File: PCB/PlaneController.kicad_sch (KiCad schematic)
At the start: 13 parts, among them J1 Conn_01x06_Pin, J2 Conn_01x04_Pin, J3 Conn_01x02, M1 Motor_Servo, M2 Motor_Servo, M3 Motor_Servo, M4 Motor_Servo, M5 Motor_Servo

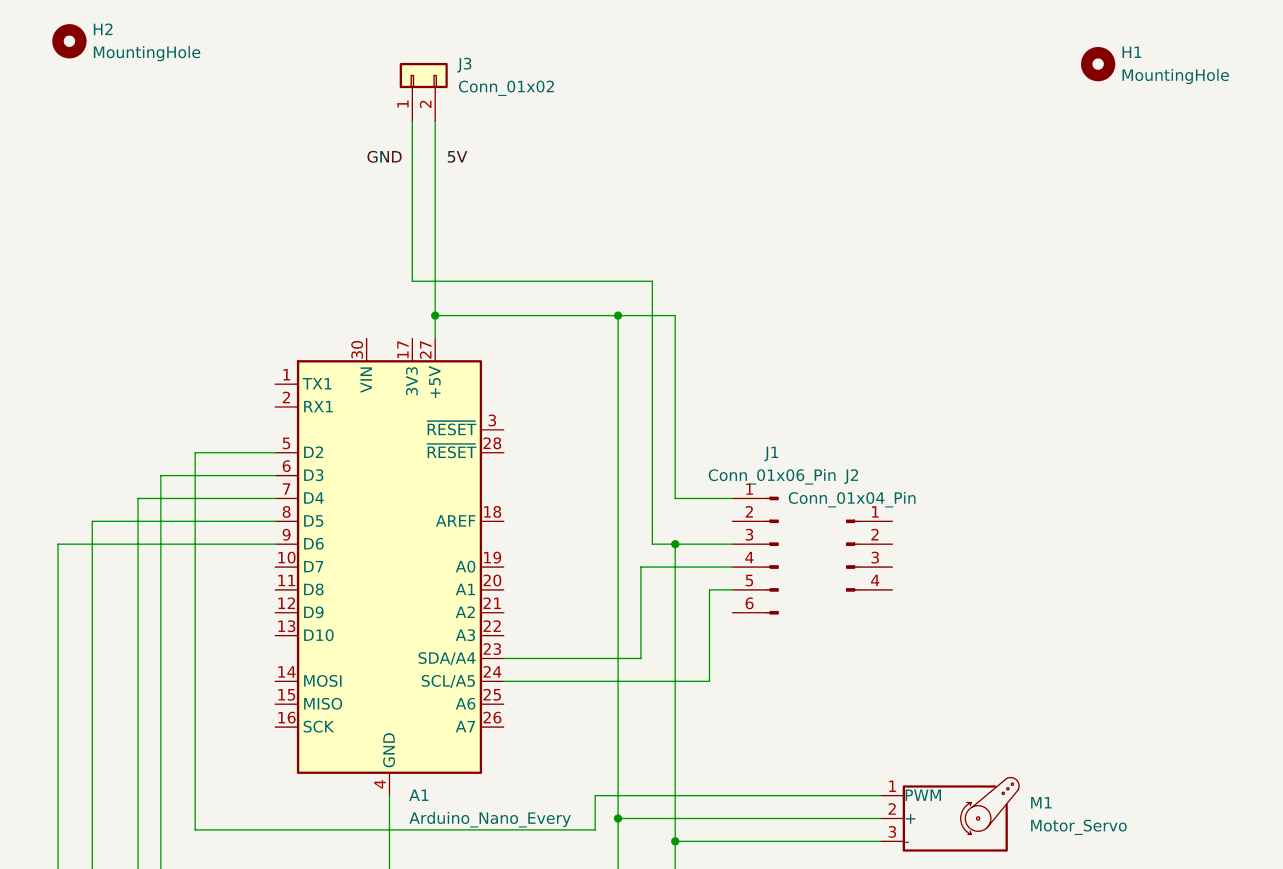
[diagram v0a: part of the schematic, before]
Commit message: Add RX and TX connections to connect to receiver via iBUS
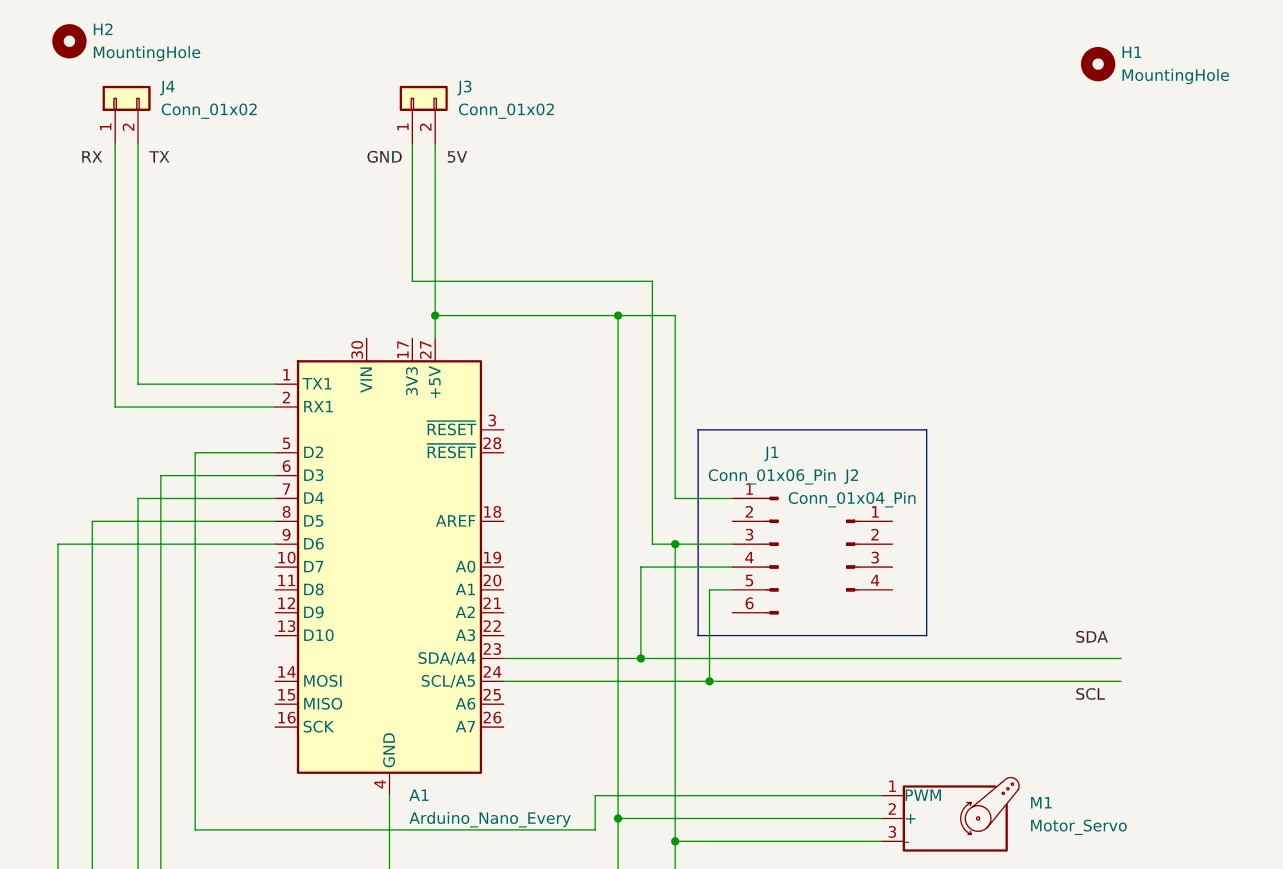
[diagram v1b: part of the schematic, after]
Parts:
- added J4: Conn_01x02, Connector_PinHeader_2.54mm:PinHeader_1x02_P2.54mm_Vertical, symbol Connector_Generic:Conn_01x02
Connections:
- net at A1.1 (TX1): now also J4.2 (Pin_2)
- net at A1.2 (RX1): now also J4.1 (Pin_1)
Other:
- moved on the sheet: J3
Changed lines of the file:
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@@
 	(paper "A4")
+	(junction
+		(at 107.95 116.84)
+		(diameter 0)
+		(color 0 0 0 0)
+	)
 	(junction
 		(at 104.14 101.6)
@@
 	)
 	(junction
+		(at 100.33 114.3)
+		(diameter 0)
+		(color 0 0 0 0)
+	)
+	(junction
 		(at 97.79 177.8)
 		(diameter 0)
@@
 	(wire
 		(pts
+			(xy 41.91 57.15) (xy 41.91 86.36)
+		)
+		(stroke
+			(width 0)
+			(type default)
+		)
+	)
+	(wire
+		(pts
 			(xy 127 142.24) (xy 46.99 142.24)
 		)
@@
 	(wire
 		(pts
+			(xy 59.69 86.36) (xy 41.91 86.36)
+		)
+		(stroke
+			(width 0)
+			(type default)
+		)
+	)
+	(wire
+		(pts
 			(xy 97.79 153.67) (xy 127 153.67)
 		)
@@
 	(wire
 		(pts
+			(xy 59.69 83.82) (xy 44.45 83.82)
+		)
+		(stroke
+			(width 0)
+			(type default)
+		)
+	)
+	(wire
+		(pts
 			(xy 104.14 180.34) (xy 127 180.34)
 		)
@@
 	(wire
 		(pts
-			(xy 74.93 54.61) (xy 74.93 72.39)
+			(xy 74.93 57.15) (xy 74.93 72.39)
 		)
 		(stroke
@@
 	(wire
 		(pts
+			(xy 44.45 57.15) (xy 44.45 83.82)
+		)
+		(stroke
+			(width 0)
+			(type default)
+		)
+	)
+	(wire
+		(pts
 			(xy 95.25 129.54) (xy 127 129.54)
 		)
@@
 	(wire
 		(pts
+			(xy 100.33 114.3) (xy 153.67 114.3)
+		)
+		(stroke
+			(width 0)
+			(type default)
+		)
+	)
+	(wire
+		(pts
 			(xy 95.25 129.54) (xy 95.25 133.35)
 		)
@@
 	(wire
 		(pts
+			(xy 107.95 116.84) (xy 153.67 116.84)
+		)
+		(stroke
+			(width 0)
+			(type default)
+		)
+	)
+	(wire
+		(pts
 			(xy 104.14 180.34) (xy 104.14 190.5)
 		)
@@
 	(wire
 		(pts
-			(xy 77.47 54.61) (xy 77.47 76.2)
+			(xy 77.47 57.15) (xy 77.47 76.2)
 		)
 		(stroke
@@
 		)
 	)
-	(label "5V"
-		(at 78.74 59.69 0)
+	(rectangle
+		(start 106.68 88.9)
+		(end 132.08 111.76)
+		(stroke
+			(width 0)
+			(type default)
+		)
+		(fill
+			(type none)
+		)
+	)
+	(label "SCL"
+		(at 148.59 119.38 0)
 		(fields_autoplaced yes)
 		(effects
@@
 		)
 	)
+	(label "5V"
+		(at 78.74 59.69 0)
+		(fields_autoplaced yes)
+		(effects
+			(font
+				(size 1.27 1.27)
+			)
+			(justify left bottom)
+		)
+	)
 	(label "GND"
 		(at 69.85 59.69 0)
+		(fields_autoplaced yes)
+		(effects
+			(font
+				(size 1.27 1.27)
+			)
+			(justify left bottom)
+		)
+	)
+	(label "TX"
+		(at 45.72 59.69 0)
+		(fields_autoplaced yes)
+		(effects
+			(font
+				(size 1.27 1.27)
+			)
+			(justify left bottom)
+		)
+	)
+	(label "RX"
+		(at 38.1 59.69 0)
+		(fields_autoplaced yes)
+		(effects
+			(font
+				(size 1.27 1.27)
+			)
+			(justify left bottom)
+		)
+	)
+	(label "SDA"
+		(at 148.59 113.03 0)
 		(fields_autoplaced yes)
 		(effects
@@
 	(symbol
 		(lib_id "Connector_Generic:Conn_01x02")
-		(at 74.93 49.53 90)
+		(at 74.93 52.07 90)
 		(unit 1)
 		(exclude_from_sim no)
@@
 		(fields_autoplaced yes)
 		(property "Reference" "J3"
-			(at 80.01 48.2599 90)
+			(at 80.01 50.7999 90)
 			(effects
 				(font
@@
 		)
 		(property "Value" "Conn_01x02"
-			(at 80.01 50.7999 90)
+			(at 80.01 53.3399 90)
 			(effects
 				(font
@@
 		)
 		(property "Footprint" "Connector_PinHeader_2.54mm:PinHeader_1x02_P2.54mm_Vertical"
-			(at 74.93 49.53 0)
+			(at 74.93 52.07 0)
 			(effects
 				(font
@@
 		)
 		(property "Datasheet" "~"
-			(at 74.93 49.53 0)
+			(at 74.93 52.07 0)
 			(effects
 				(font
@@
 		)
 		(property "Description" "Generic connector, single row, 01x02, script generated (kicad-library-utils/schlib/autogen/connector/)"
-			(at 74.93 49.53 0)
+			(at 74.93 52.07 0)
 			(effects
 				(font
@@
 					(unit 1)
 				)
+			)
+		)
+	)
+	(symbol
+		(lib_id "Connector_Generic:Conn_01x02")
+		(at 41.91 52.07 90)
+		(unit 1)
+		(exclude_from_sim no)
+		(in_bom yes)
+		(on_board yes)
+		(dnp no)
+		(fields_autoplaced yes)
+		(property "Reference" "J4"
+			(at 46.99 50.7999 90)
+			(effects
+				(font
+					(size 1.27 1.27)
+				)
+				(justify right)
+			)
+		)
+		(property "Value" "Conn_01x02"
+			(at 46.99 53.3399 90)
+			(effects
+				(font
+					(size 1.27 1.27)
+				)
+				(justify right)
+			)
+		)
+		(property "Footprint" "Connector_PinHeader_2.54mm:PinHeader_1x02_P2.54mm_Vertical"
+			(at 41.91 52.07 0)
+			(effects
+				(font
+					(size 1.27 1.27)
+				)
+				(hide yes)
+			)
+		)
+		(property "Datasheet" "~"
+			(at 41.91 52.07 0)
+			(effects
+				(font
+					(size 1.27 1.27)
+				)
+				(hide yes)
+			)
+		)
+		(property "Description" "Generic connector, single row, 01x02, script generated (kicad-library-utils/schlib/autogen/connector/)"
+			(at 41.91 52.07 0)
+			(effects
+				(font
+					(size 1.27 1.27)
+				)
+				(hide yes)
+			)
+		)
+		(pin "1"
+		)
+		(pin "2"
+		)
+		(instances
+			(project "PlaneController"
+				(path "/f475b102-a671-4895-926c-dd521b2271ca"
+					(reference "J4")
+					(unit 1)
+				)

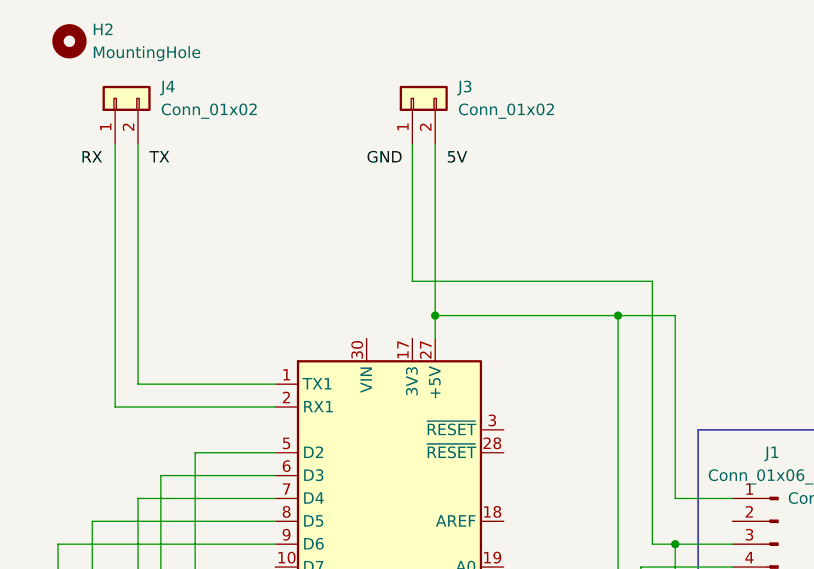
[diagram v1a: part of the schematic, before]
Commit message: Add connection to receiver using 3x1 pin for iBUS, Vcc and GND
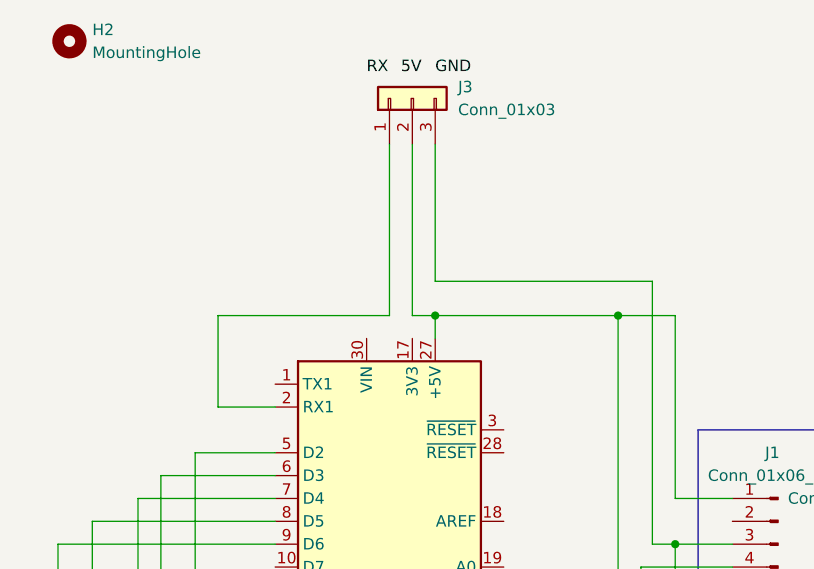
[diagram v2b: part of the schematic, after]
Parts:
- removed J3, J4: Conn_01x02, Connector_PinHeader_2.54mm:PinHeader_1x02_P2.54mm_Vertical, symbol Connector_Generic:Conn_01x02
- added J3: Conn_01x03, Connector_PinHeader_2.54mm:PinHeader_1x03_P2.54mm_Vertical, symbol Connector_Generic:Conn_01x03
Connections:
- net at A1.27 (+5V), J1.1 (Pin_1), M1.2 (+)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: now also J3.2 (Pin_2)
- net at A1.29 (GND), A1.4 (GND), J1.3 (Pin_3)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: now also J3.3 (Pin_3)
- net at A1.2 (RX1): now also J3.1 (Pin_1)
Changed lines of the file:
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@@
+	)
+	(junction
+		(at 77.47 76.2)
+		(diameter 0)
+		(color 0 0 0 0)
 	)
 	(junction
@@
 	)
 	(junction
-		(at 77.47 76.2)
-		(diameter 0)
-		(color 0 0 0 0)
-	)
-	(junction
 		(at 104.14 167.64)
 		(diameter 0)
@@
 	(wire
 		(pts
+			(xy 72.39 57.15) (xy 72.39 76.2)
+		)
+		(stroke
+			(width 0)
+			(type default)
+		)
+	)
+	(wire
+		(pts
 			(xy 97.79 76.2) (xy 77.47 76.2)
 		)
@@
 	(wire
 		(pts
+			(xy 72.39 76.2) (xy 53.34 76.2)
+		)
+		(stroke
+			(width 0)
+			(type default)
+		)
+	)
+	(wire
+		(pts
 			(xy 104.14 167.64) (xy 127 167.64)
 		)
@@
 	(wire
 		(pts
-			(xy 41.91 57.15) (xy 41.91 86.36)
-		)
-		(stroke
-			(width 0)
-			(type default)
-		)
-	)
-	(wire
-		(pts
 			(xy 127 142.24) (xy 46.99 142.24)
 		)
@@
 	(wire
 		(pts
-			(xy 74.93 72.39) (xy 101.6 72.39)
-		)
-		(stroke
-			(width 0)
-			(type default)
-		)
-	)
-	(wire
-		(pts
 			(xy 104.14 156.21) (xy 104.14 167.64)
 		)
@@
 	(wire
 		(pts
-			(xy 59.69 86.36) (xy 41.91 86.36)
+			(xy 74.93 76.2) (xy 77.47 76.2)
 		)
 		(stroke
@@
 	(wire
 		(pts
-			(xy 59.69 83.82) (xy 44.45 83.82)
+			(xy 101.6 72.39) (xy 77.47 72.39)
 		)
 		(stroke
@@
 	(wire
 		(pts
-			(xy 74.93 57.15) (xy 74.93 72.39)
-		)
-		(stroke
-			(width 0)
-			(type default)
-		)
-	)
-	(wire
-		(pts
 			(xy 101.6 101.6) (xy 104.14 101.6)
 		)
@@
 	(wire
 		(pts
-			(xy 44.45 57.15) (xy 44.45 83.82)
+			(xy 74.93 57.15) (xy 74.93 76.2)
 		)
 		(stroke
@@
 	(wire
 		(pts
+			(xy 77.47 57.15) (xy 77.47 72.39)
+		)
+		(stroke
+			(width 0)
+			(type default)
+		)
+	)
+	(wire
+		(pts
 			(xy 100.33 114.3) (xy 153.67 114.3)
 		)
@@
 	(wire
 		(pts
+			(xy 53.34 76.2) (xy 53.34 86.36)
+		)
+		(stroke
+			(width 0)
+			(type default)
+		)
+	)
+	(wire
+		(pts
 			(xy 39.37 162.56) (xy 39.37 99.06)
 		)
@@
 	(wire
 		(pts
+			(xy 53.34 86.36) (xy 59.69 86.36)
+		)
+		(stroke
+			(width 0)
+			(type default)
+		)
+	)
+	(wire
+		(pts
 			(xy 104.14 180.34) (xy 104.14 190.5)
 		)
@@
 		(pts
 			(xy 44.45 96.52) (xy 59.69 96.52)
-		)
-		(stroke
-			(width 0)
-			(type default)
-		)
-	)
-	(wire
-		(pts
-			(xy 77.47 57.15) (xy 77.47 76.2)
 		)
 		(stroke
@@
 	)
 	(label "5V"
-		(at 78.74 59.69 0)
+		(at 73.66 49.53 0)
 		(fields_autoplaced yes)
 		(effects
@@
 	)
 	(label "GND"
-		(at 69.85 59.69 0)
+		(at 77.47 49.53 0)
 		(fields_autoplaced yes)
 		(effects
@@
 		)
 	)
-	(label "TX"
-		(at 45.72 59.69 0)
-		(fields_autoplaced yes)
-		(effects
-			(font
-				(size 1.27 1.27)
-			)
-			(justify left bottom)
-		)
-	)
 	(label "RX"
-		(at 38.1 59.69 0)
+		(at 69.85 49.53 0)
 		(fields_autoplaced yes)
 		(effects
@@
 				(path "/f475b102-a671-4895-926c-dd521b2271ca"
 					(reference "M2")
-					(unit 1)
-				)
-			)
-		)
-	)
-	(symbol
-		(lib_id "Connector_Generic:Conn_01x02")
-		(at 74.93 52.07 90)
-		(unit 1)
-		(exclude_from_sim no)
-		(in_bom yes)
-		(on_board yes)
-		(dnp no)
-		(fields_autoplaced yes)
-		(property "Reference" "J3"
-			(at 80.01 50.7999 90)
-			(effects
-				(font
-					(size 1.27 1.27)
-				)
-				(justify right)
-			)
-		)
-		(property "Value" "Conn_01x02"
-			(at 80.01 53.3399 90)
-			(effects
-				(font
-					(size 1.27 1.27)
-				)
-				(justify right)
-			)
-		)
-		(property "Footprint" "Connector_PinHeader_2.54mm:PinHeader_1x02_P2.54mm_Vertical"
-			(at 74.93 52.07 0)
-			(effects
-				(font
-					(size 1.27 1.27)
-				)
-				(hide yes)
-			)
-		)
-		(property "Datasheet" "~"
-			(at 74.93 52.07 0)
-			(effects
-				(font
-					(size 1.27 1.27)
-				)
-				(hide yes)
-			)
-		)
-		(property "Description" "Generic connector, single row, 01x02, script generated (kicad-library-utils/schlib/autogen/connector/)"
-			(at 74.93 52.07 0)
-			(effects
-				(font
-					(size 1.27 1.27)
-				)
-				(hide yes)
-			)
-		)
-		(pin "1"
-		)
-		(pin "2"
-		)
-		(instances
-			(project ""
-				(path "/f475b102-a671-4895-926c-dd521b2271ca"
-					(reference "J3")
 					(unit 1)
 				)
@@
 	)
 	(symbol
-		(lib_id "Connector_Generic:Conn_01x02")
-		(at 41.91 52.07 90)
-		(unit 1)
-		(exclude_from_sim no)
-		(in_bom yes)
-		(on_board yes)
-		(dnp no)
-		(fields_autoplaced yes)
-		(property "Reference" "J4"
-			(at 46.99 50.7999 90)
-			(effects
-				(font
-					(size 1.27 1.27)
-				)
-				(justify right)
-			)
-		)
-		(property "Value" "Conn_01x02"
-			(at 46.99 53.3399 90)
-			(effects
-				(font
-					(size 1.27 1.27)
-				)
-				(justify right)
-			)
-		)
-		(property "Footprint" "Connector_PinHeader_2.54mm:PinHeader_1x02_P2.54mm_Vertical"
-			(at 41.91 52.07 0)
-			(effects
-				(font
-					(size 1.27 1.27)
-				)
-				(hide yes)
-			)
-		)
-		(property "Datasheet" "~"
-			(at 41.91 52.07 0)
-			(effects
-				(font
-					(size 1.27 1.27)
-				)
-				(hide yes)
-			)
-		)
-		(property "Description" "Generic connector, single row, 01x02, script generated (kicad-library-utils/schlib/autogen/connector/)"
-			(at 41.91 52.07 0)
-			(effects
-				(font
-					(size 1.27 1.27)
-				)
-				(hide yes)
-			)
-		)
-		(pin "1"
-		)
-		(pin "2"
-		)
-		(instances
-			(project "PlaneController"
-				(path "/f475b102-a671-4895-926c-dd521b2271ca"
-					(reference "J4")
-					(unit 1)
-				)
-			)
-		)
-	)
-	(symbol
 		(lib_id "Mechanical:MountingHole")
 		(at 151.13 48.26 0)
@@
 					(unit 1)
 				)
+			)
+		)
+	)
+	(symbol
+		(lib_id "Connector_Generic:Conn_01x03")
+		(at 74.93 52.07 90)
+		(unit 1)
+		(exclude_from_sim no)
+		(in_bom yes)
+		(on_board yes)
+		(dnp no)
+		(fields_autoplaced yes)
+		(property "Reference" "J3"
+			(at 80.01 50.7999 90)
+			(effects
+				(font
+					(size 1.27 1.27)
+				)
+				(justify right)
+			)
+		)
+		(property "Value" "Conn_01x03"
+			(at 80.01 53.3399 90)
+			(effects
+				(font
+					(size 1.27 1.27)
+				)
+				(justify right)
+			)
+		)
+		(property "Footprint" "Connector_PinHeader_2.54mm:PinHeader_1x03_P2.54mm_Vertical"
+			(at 74.93 52.07 0)
+			(effects
+				(font
+					(size 1.27 1.27)
+				)
+				(hide yes)
+			)
+		)
+		(property "Datasheet" "~"
+			(at 74.93 52.07 0)
+			(effects
+				(font
+					(size 1.27 1.27)
+				)
+				(hide yes)
+			)
+		)
+		(property "Description" "Generic connector, single row, 01x03, script generated (kicad-library-utils/schlib/autogen/connector/)"
+			(at 74.93 52.07 0)
+			(effects
+				(font
+					(size 1.27 1.27)
+				)
+				(hide yes)
+			)
+		)
+		(pin "1"
+		)
+		(pin "2"
+		)
+		(pin "3"
+		)
+		(instances
+			(project ""
+				(path "/f475b102-a671-4895-926c-dd521b2271ca"
+					(reference "J3")
+					(unit 1)
+				)
